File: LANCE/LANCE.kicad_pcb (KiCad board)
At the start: 2 copper layers, 87 x 148 mm, 65 parts, among them J1 4s Batt, J12 Sparkmax 1 Pwr, J13 Lin Actuator 1 (Large), J15 Lasers, J16 SHT30, J17 Lin Actuator 2 (Small), J19 Sparkmax PWM 1, J2 12V, J20 Sparkmax PWM 2, J21 Sparkmax 2 Pwr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

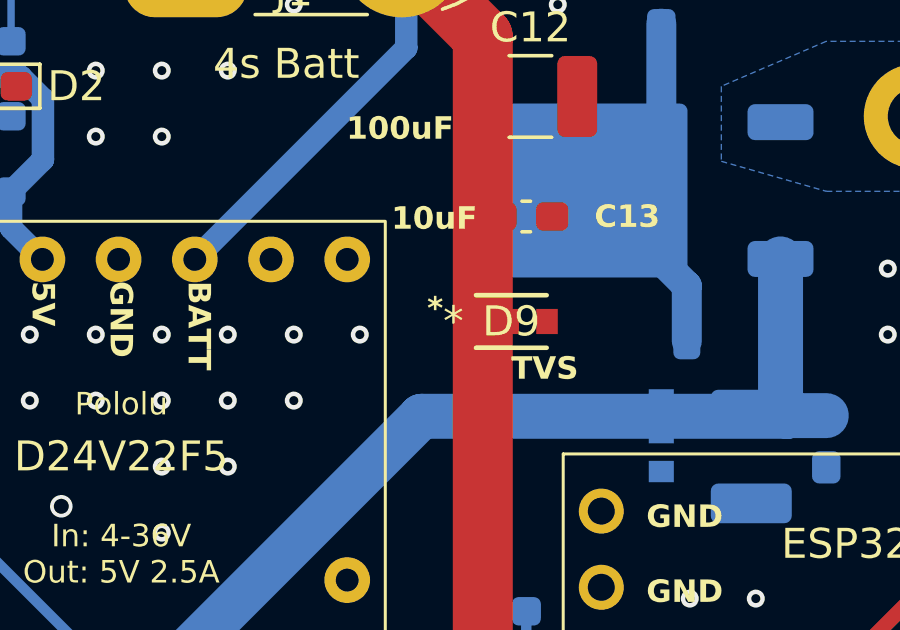
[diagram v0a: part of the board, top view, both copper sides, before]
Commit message: LANCE 2026 r1.01
A1 Pin 8 pad connection changed to solid
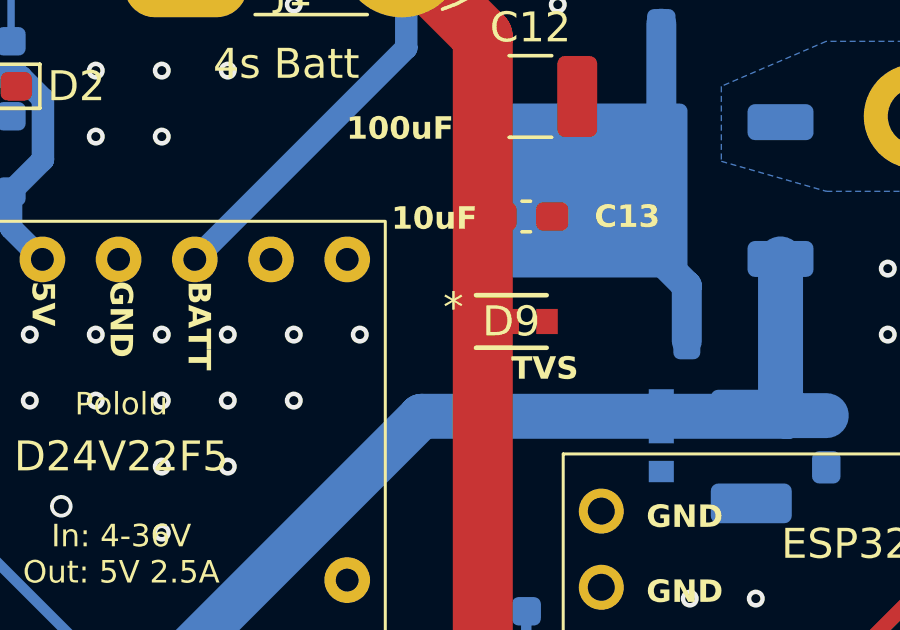
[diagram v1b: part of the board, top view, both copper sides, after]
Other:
- board text removed: "*"
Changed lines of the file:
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@@
 		(title "LANCE 2026")
 		(date "2026-04-21")
-		(rev "1")
+		(rev "1.01")
 		(company "UAH SHC ASTRA")
 		(comment 1 "Created by Robert Geren")
@@
 			(disableapertmacros no)
 			(usegerberextensions yes)
-			(usegerberattributes no)
-			(usegerberadvancedattributes no)
+			(usegerberattributes yes)
+			(usegerberadvancedattributes yes)
 			(creategerberjobfile no)
 			(dashed_line_dash_ratio 12.000000)
@@
 			(sketchdnponfab yes)
 			(crossoutdnponfab yes)
-			(subtractmaskfromsilk yes)
+			(subtractmaskfromsilk no)
 			(outputformat 1)
 			(mirror no)
 			(drillshape 0)
 			(scaleselection 1)
-			(outputdirectory "DIGIT V2 GERBERS/")
+			(outputdirectory "LANCE Gerbers/")
 		)
 	)
@@
 		)
 		(fp_text user "*"
-			(at -1.9304 0 0)
-			(layer "F.SilkS")
-			(effects
-				(font
-					(size 1 1)
-					(thickness 0.15)
-				)
-			)
-		)
-		(fp_text user "*"
-			(at -1.9304 0 0)
-			(unlocked yes)
+			(at -1.9304 -0.462749 0)
 			(layer "F.SilkS")
 			(effects
@@
 			(pinfunction "GND")
 			(pintype "power_in")
+			(zone_connect 2)
 		)
 		(pad "9" thru_hole circle
@@
 		)
 		(fp_text user "*"
-			(at -1.9304 0 90)
-			(layer "B.SilkS")
-			(effects
-				(font
-					(size 1 1)
-					(thickness 0.15)
-				)
-				(justify mirror)
-			)
-		)
-		(fp_text user "*"
-			(at -1.9304 0 90)
-			(unlocked yes)
+			(at -1.9304 0.95 90)
 			(layer "B.SilkS")
 			(effects
@@
 		)
 	)
-	(gr_text "*"
-		(at 74.6438 62.962749 0)
-		(layer "F.SilkS")
-		(effects
-			(font
-				(size 0.75 0.75)
-				(thickness 0.125)
-				(bold yes)
-			)
-			(justify left bottom)
-		)
-	)
 	(gr_text "Fan Pwr"
 		(at 101.45 176.7 0)
@@
 			)
 			(justify left bottom mirror)
-		)
-	)
-	(gr_text "*"
-		(at 81.5737 65.589349 0)
-		(layer "B.SilkS")
-		(effects
-			(font
-				(size 0.75 0.75)
-				(thickness 0.125)
-				(bold yes)
-			)
-			(justify left bottom mirror)

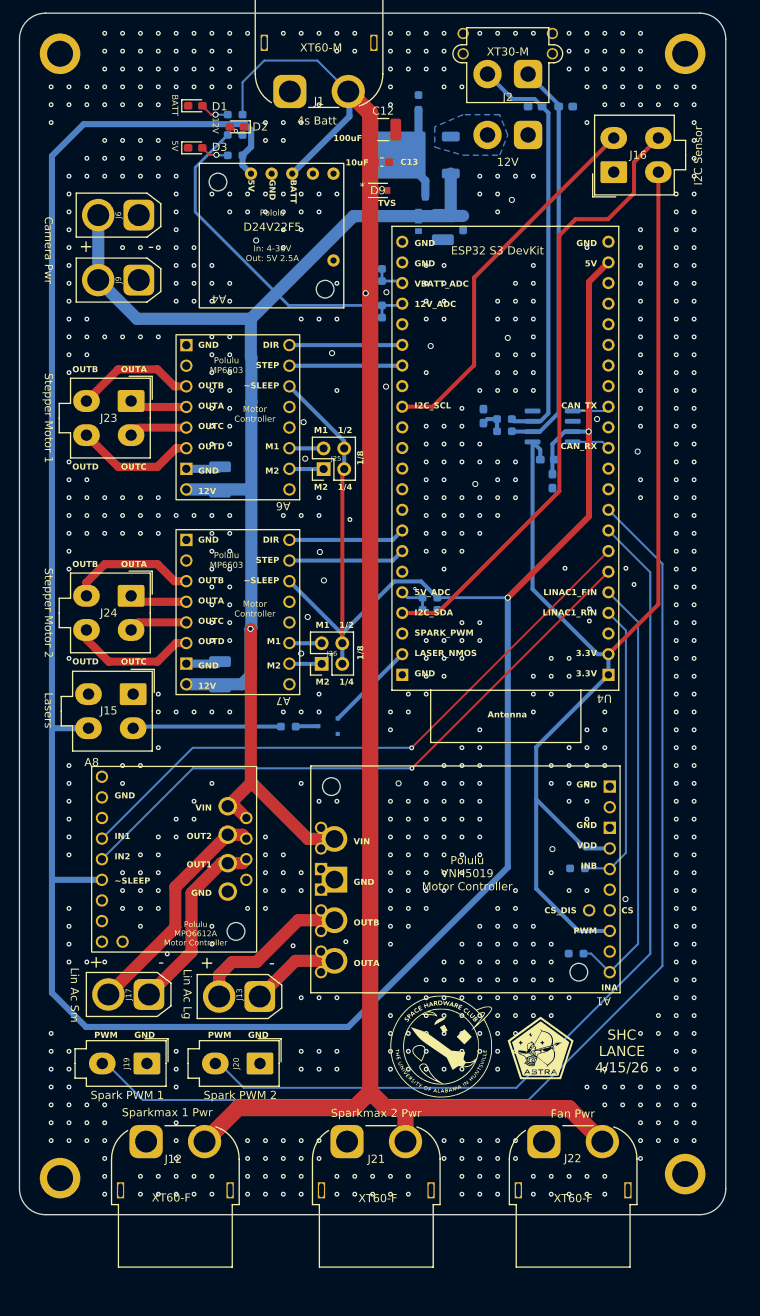
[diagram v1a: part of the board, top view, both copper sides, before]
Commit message: LANCE 2026 r1.02
Changed nSLEEP on MP6603 (x2) and on MPQ6612A to 3.3V, moved CAN_TX to non-strapping pin 9 on ESP32, changed SHT30 connector to I2C connector convention used on Core and Antenna, moved SHT30 connector to bottom right, rerouted 5V trace, added 63uF (x4) bank to battery trace to lessen voltage sag, grouped ground vias, and added Gerbers/Drill files
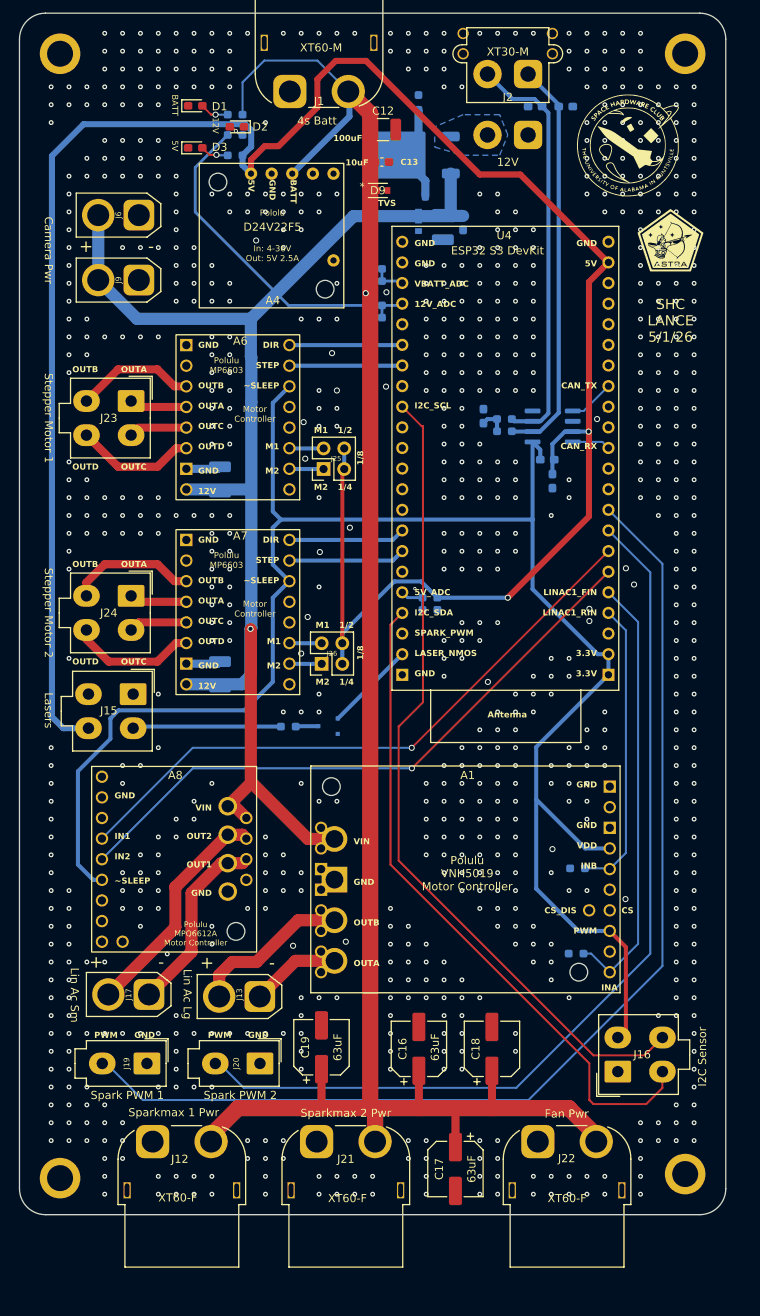
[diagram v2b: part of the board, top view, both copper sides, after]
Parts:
- added C16: 63uF, Capacitor_SMD:CP_Elec_6.3x7.7, F.Cu at (82.5, 168.7)
- added C17: 63uF, Capacitor_SMD:CP_Elec_6.3x7.7, F.Cu at (87.0, 183.5)
- added C18: 63uF, Capacitor_SMD:CP_Elec_6.3x7.7, F.Cu at (91.5, 168.7)
- added C19: 63uF, Capacitor_SMD:CP_Elec_6.3x7.7, F.Cu at (70.5, 168.5)
- G***: footprint FAERIE:SHC_Logo -> LANCE:SHC_Logo
- G***: footprint FAERIE:ASTRA_Logo -> LANCE:ASTRA_Logo
- moved G*** 113.4 mm to (108.5, 57.5)
- moved J16 110.8 mm to (107.0, 171.5)
- moved G*** 100.8 mm to (113.5, 69.0)
- moved J21 3.75 mm to (69.9, 180.1)
- moved J12 0.80 mm to (49.7, 180.1)
- moved J22 0.75 mm to (97.2, 180.1)
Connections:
- A6 pad 6: +5V -> +3.3V
- A7 pad 6: +5V -> +3.3V
- A8 pad 6: +5V -> +3.3V
- J16 pad 2: /I2C_SCL -> +3.3V
- J16 pad 3: +3.3V -> /I2C_SDA
- J16 pad 4: /I2C_SDA -> /I2C_SCL
- U4 pad 46: /CAN_TX -> unconnected-(U4-GPIO46-Pad46)
- U4 pad 9: unconnected-(U4-GPIO9-Pad9) -> /CAN_TX
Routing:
- net +5V: track 371.8 -> 276.3 mm
- net +3.3V: track 151.0 -> 219.4 mm
- net /I2C_SCL: track 46.1 -> 101.6 mm
- net +BATT: track 217.3 -> 236.5 mm
- net /I2C_SDA: track 76.5 -> 82.8 mm
- net /CAN_TX: track 4.62 -> 5.67 mm
- net unconnected-(U4-GPIO46-Pad46): track 0.00 -> 0.74 mm
- net GND: vias 812 -> 851
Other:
- board text added: "63uF"
- board text added: "SHC LANCE 5/1/26"
- board text removed: "SHC LANCE 4/15/26"
